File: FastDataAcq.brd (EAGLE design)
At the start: 160 x 100 mm, 225 parts, among them IC1 LT1963AEQ, IC2 FT230XQ, IC3 ADCMP553BRMZ, J1 MICRO-FIT_3.0_2POS_RA_SMD, J2 USB_MICROAB_SMT, X1 87832-14, X2 SMA-142-0701-801/806, X3 SMA-142-0701-801/806, Y1 SI530-500, Y2 100MHz, Y3 DNP

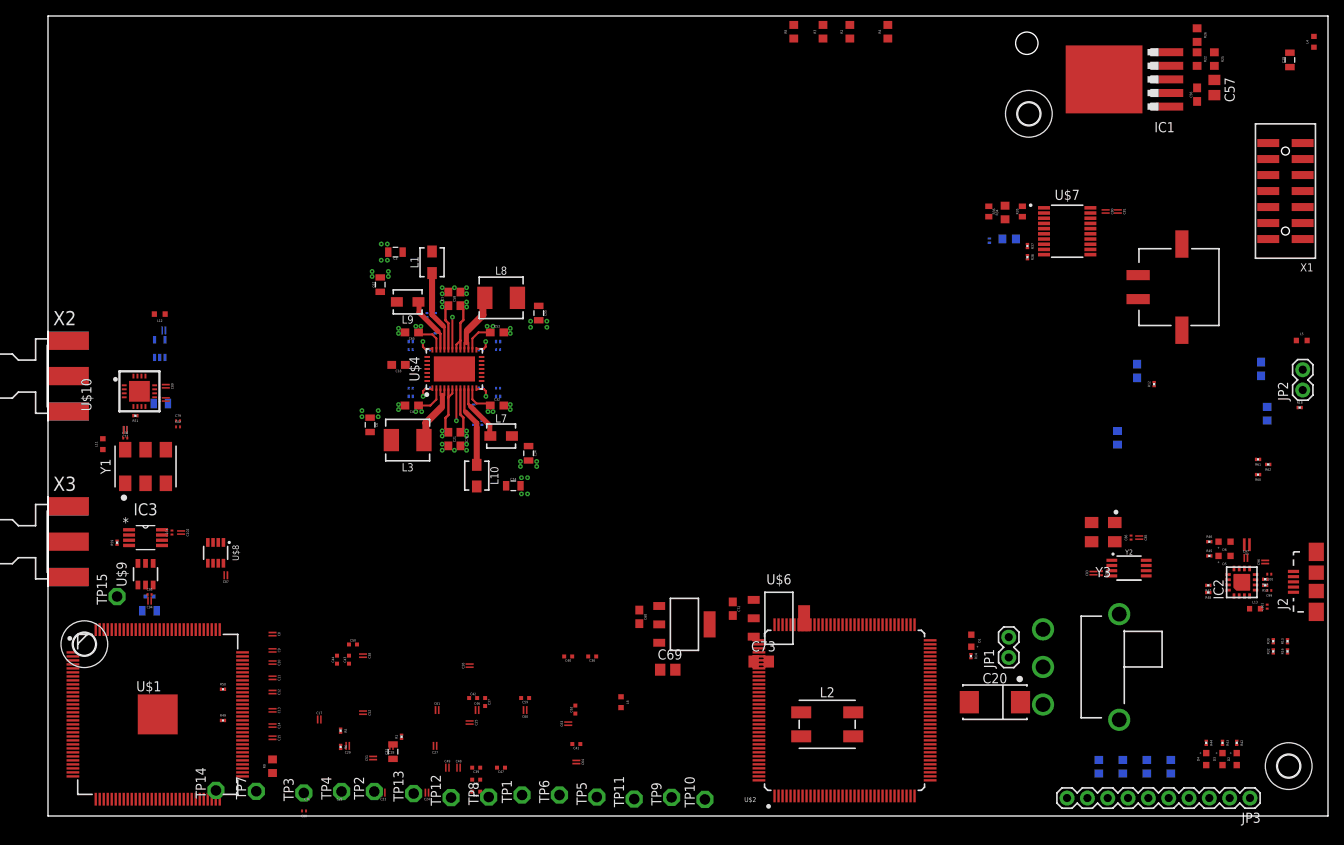
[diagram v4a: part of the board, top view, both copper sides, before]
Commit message: Component placement semi-finalized
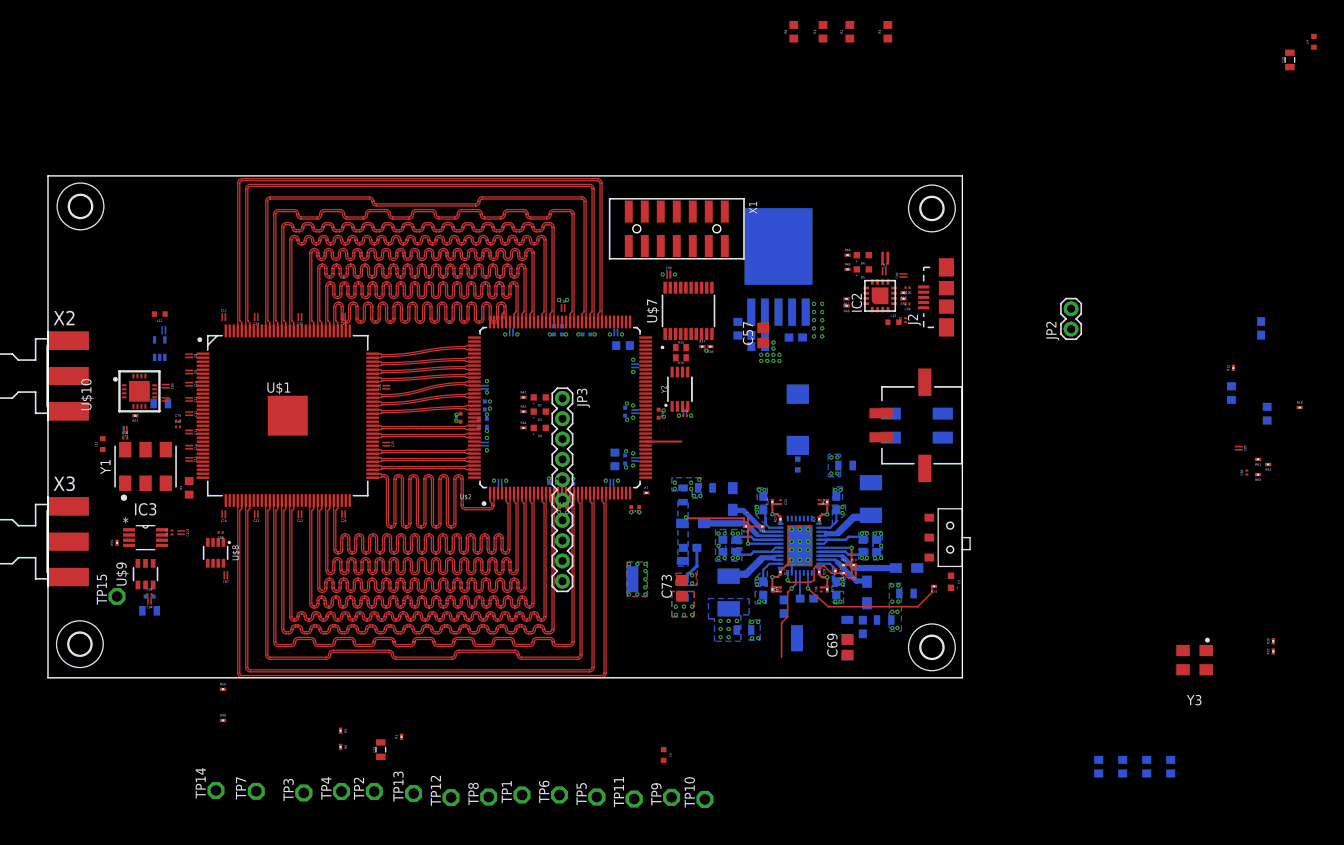
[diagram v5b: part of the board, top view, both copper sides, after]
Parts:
- removed JP1: JUMPER-2PTH, SparkFun-Passives:1X02
- removed U$3: SLIDER_SPDT_1101M2S3AQE2, Schuyler:C_AND_K_1101M2S3AQE2
- added S1: SLIDER_SPDT_AYZ0102AGRLC, Schuyler:AYZ0102AGRLC
- moved H4 166.4 mm to (4.06, 76.2), turned to 0 degrees
- moved H3 135.9 mm to (3.99, 21.5)
- moved H2 119.1 mm to (110.5, 75.9)
- moved JP3 99.4 mm to (64.3, 52.2), turned to 270 degrees
- moved R42 99.1 mm to (59.4, 52.3), turned to 0 degrees
- moved D2 98.2 mm to (61.5, 52.3), turned to 180 degrees
- moved R43 96.7 mm to (59.4, 50.5), turned to 0 degrees
- moved D3 95.8 mm to (61.5, 50.5), turned to 180 degrees
- moved R44 94.0 mm to (59.4, 48.5), turned to 0 degrees
- moved D4 93.0 mm to (61.5, 48.5), turned to 180 degrees
- moved C3 76.8 mm to (107.3, 27.8), flipped to the bottom, turned to 0 degrees
- moved H1 76.4 mm to (110.5, 21.1), flipped to the top
- moved X1 76.2 mm to (78.6, 73.4), turned to 180 degrees
- moved C67 75.7 mm to (104.5, 24.5), flipped to the bottom, turned to 180 degrees
- moved L1 70.6 mm to (107.3, 31.0), flipped to the bottom, turned to 180 degrees
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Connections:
- net N$12 renamed S1EN
- net N$16 renamed S4EN
- removed net N$1: JP1.2, L2.P$4, U$3.P$1
- removed net N$17: C20.P$2, JP1.1, L5.P$1, R14.2, U$3.P$2
- removed net POWER_IN+: J1.P$2, L2.P$1
- removed net POWER_IN-: J1.P$1, L2.P$2
- new net N$24: C20.P$1, L2.P$3, L5.P$1
- new net N$34: J1.P$1, L2.P$1
- new net N$35: J1.P$2, L2.P$2
- new net PWR_ENABLE: R14.2, S1.P$2, U$4.P$13, U$4.P$33
- net GND: now also C20.P$2, L2.P$4, S1.P$1; no longer C20.P$1, L2.P$3
- net VIN: now also S1.P$3; no longer U$4.P$13, U$4.P$33
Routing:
- net DQD0+: track 0.00 -> 90.6 mm
- net DQD0-: track 0.00 -> 90.0 mm
- net DQD1+: track 0.00 -> 86.6 mm
- net DQD1-: track 0.00 -> 86.1 mm
- net DID0+: track 0.00 -> 81.8 mm
- net DID0-: track 0.00 -> 81.3 mm
- net DQD2+: track 0.00 -> 80.9 mm
- net DQD2-: track 0.00 -> 80.4 mm
- net DQ2+: track 0.00 -> 79.7 mm
- net DQD3+: track 0.00 -> 79.6 mm
- net DQ2-: track 0.00 -> 79.4 mm
- net DQD3-: track 0.00 -> 79.1 mm
- net DID1+: track 0.00 -> 78.4 mm
- net DQ1+: track 0.00 -> 78.2 mm
- net DQ0+: track 0.00 -> 78.0 mm
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- added copper zone on layer 16, net 3V3
- added copper zone on layer 1, net 3V3A
- added copper zone on layer 16, net 3V3A
- added copper zone on layer 16, net 3V6_PRE3V3
- added copper zone on layer 1, net GND
- added copper zone on layer 16, net GND
- added copper zone on layer 2, net GND
- added copper zone on layer 16, net VIN
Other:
- board size 160 x 100 mm -> 114.3 x 62.7 mm

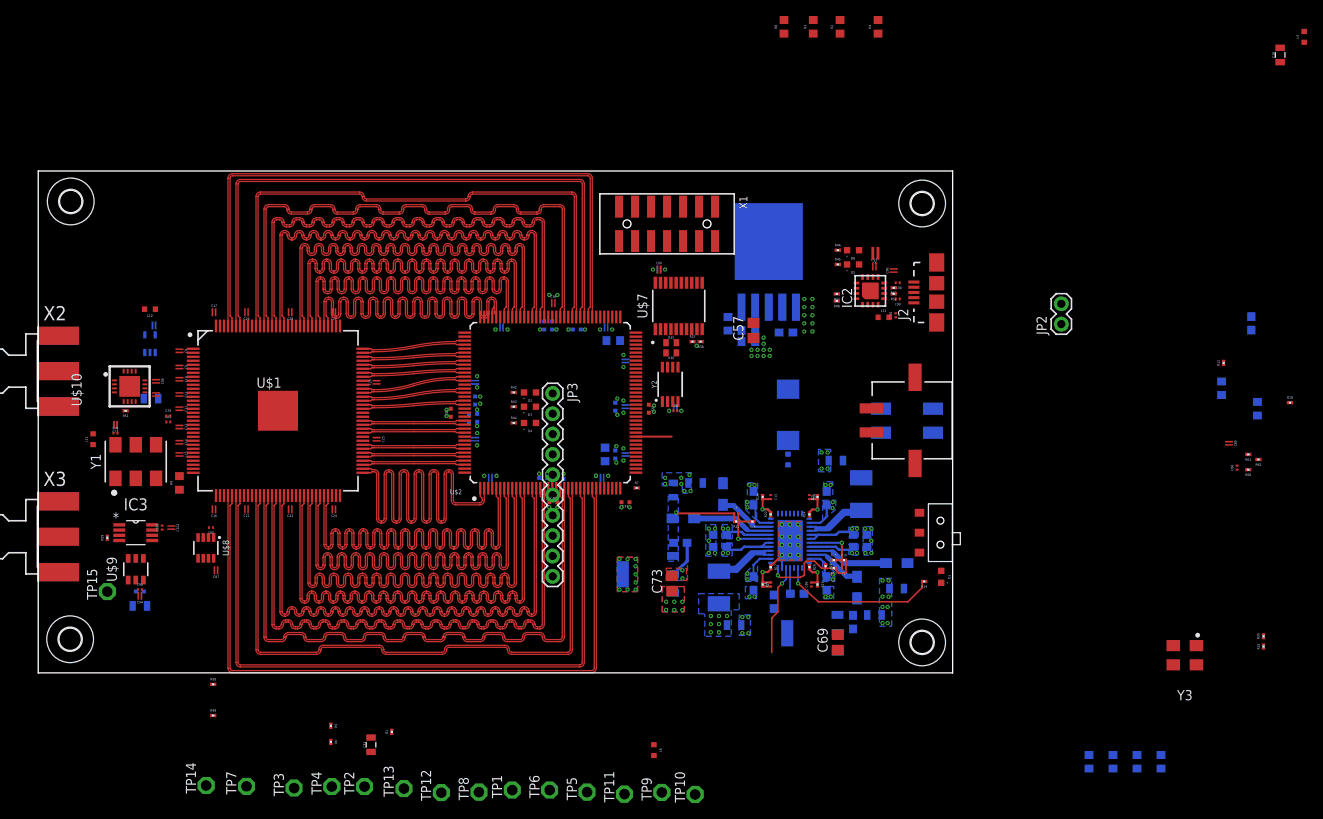
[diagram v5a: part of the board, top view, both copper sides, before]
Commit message: Board layout almost complete.
Power plane almost routes all the power correctly.
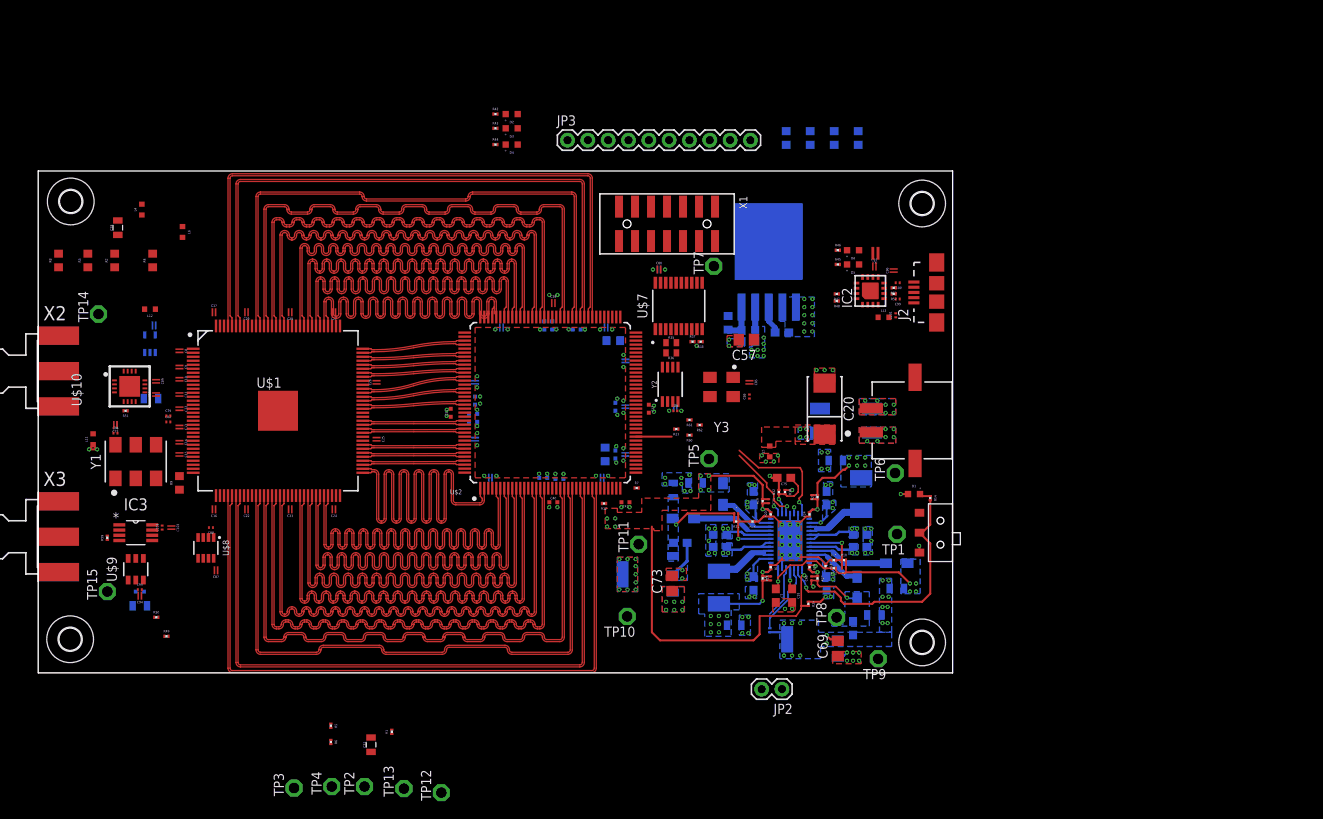
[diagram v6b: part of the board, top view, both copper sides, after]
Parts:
- R23, R28: value NA -> 523K; device rcl:R0603 -> rcl:R0201
- moved C19 146.9 mm to (9.95, 72.9)
- moved L4 146.9 mm to (13.0, 75.2)
- moved R2 95.3 mm to (9.55, 68.8)
- moved R3 95.3 mm to (6.20, 68.8)
- moved R4 95.3 mm to (14.3, 68.8)
- moved R8 95.3 mm to (2.54, 68.8)
- moved L6 87.6 mm to (18.0, 72.4)
- moved TP7 87.4 mm to (84.5, 68.1)
- moved R54 86.7 mm to (99.5, 84.1)
- moved R55 86.7 mm to (96.5, 84.1)
- moved R56 86.7 mm to (93.5, 84.1)
- moved R57 86.7 mm to (102.5, 84.1)
- moved R12 79.4 mm to (70.7, 38.4), turned to 180 degrees
- moved R18 71.0 mm to (91.4, 22.6), flipped to the bottom, turned to 90 degrees
- moved R60 70.0 mm to (81.4, 47.0)
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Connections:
- net N$6 renamed S_MODE
- net S4EN renamed S3EN
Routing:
- net ANALOG_PWR_EN: track 0.00 -> 41.8 mm, vias 0 -> 1
- net GND: track 8.26 -> 37.8 mm, vias 87 -> 106
- net PWR_ENABLE: track 19.8 -> 46.5 mm, vias 1 -> 2
- net 2V8_2V5PRE: track 0.00 -> 22.2 mm, vias 0 -> 3
- net ADC_PWR_EN: track 0.00 -> 14.6 mm, vias 0 -> 1
- net PGOOD: track 0.00 -> 10.3 mm, vias 0 -> 1
- net 1V8: track 0.00 -> 9.75 mm, vias 9 -> 17
- net S_MODE: track 0.00 -> 9.00 mm
- net 1V2: track 3.26 -> 11.8 mm, vias 4 -> 8
- net 3V3: track 1.02 -> 9.18 mm, vias 18 -> 19
- net S3EN: track 0.00 -> 7.44 mm, vias 0 -> 1
- net 2V3_1V9PRE: track 0.00 -> 7.12 mm, vias 10 -> 16
- net S_TEMP: track 11.3 -> 6.59 mm, vias 1 -> 0
- net N$14: track 0.00 -> 4.72 mm
- net 1V9: track 0.00 -> 4.32 mm, vias 0 -> 8
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- added copper zone on layer 1, net 1V2
- added copper zone on layer 16, net 1V2
- added copper zone on layer 3, net 1V2
- added copper zone on layer 1, net 1V8
- added copper zone on layer 16, net 1V8
- added copper zone on layer 3, net 1V8
- added copper zone on layer 16, net 1V9
- added copper zone on layer 3, net 1V9
- added copper zone on layer 3, net 1V9A
- added copper zone on layer 3, net 1V9D
- added copper zone on layer 16, net 2V3_1V9PRE
- added copper zone on layer 3, net 2V3_1V9PRE
- added copper zone on layer 1, net 2V5
- added copper zone on layer 3, net 2V5
- added copper zone on layer 16, net 2V8_2V5PRE
- added copper zone on layer 3, net 3V3
- added copper zone on layer 3, net 3V3A
- added copper zone on layer 1, net N$24
- added copper zone on layer 16, net N$24
- added copper zone on layer 1, net N$34
- added copper zone on layer 16, net N$34
- added copper zone on layer 1, net N$35
- added copper zone on layer 16, net N$35
- added copper zone on layer 1, net VIN
- added copper zone on layer 3, net VIN

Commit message: Continued board layout
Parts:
- removed JP2: JUMPER-2PTH, SparkFun-Passives:1X02
- removed JP3: M10", SparkFun-Connectors:1X10
- added J3: HEADER_0.1"_10P_2R_SMT, Schuyler:HEADER_10P_2R_SMT
- added R40: 0, rcl:R0603
- moved R54 106.8 mm to (14.9, 18.9)
- moved R57 106.7 mm to (17.7, 19.4)
- moved R56 106.2 mm to (9.17, 19.6)
- moved R55 106.0 mm to (12.4, 19.6)
- moved TP13 82.1 mm to (51.3, 84.7)
- moved TP10 72.7 mm to (1.99, 12.1)
- moved TP7 70.7 mm to (15.6, 84.1)
- moved TP4 56.7 mm to (93.2, 8.01)
- moved R42 48.0 mm to (105.2, 86.4)
- moved R43 48.0 mm to (105.2, 84.6)
- moved R44 48.0 mm to (105.2, 82.5)
- moved D2 48.0 mm to (107.2, 86.4)
- moved D3 48.0 mm to (107.2, 84.6)
- moved D4 48.0 mm to (107.2, 82.5)
- moved TP5 40.5 mm to (124.2, 41.5)
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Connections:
- net 3V3: now also J3.P$1; no longer JP3.10
- net FPGA_GPIO1: now also J3.P$9; no longer JP3.2
- net FPGA_GPIO2: now also J3.P$8; no longer JP3.3
- net FPGA_GPIO3: now also J3.P$7; no longer JP3.4
- net FPGA_GPIO4: now also J3.P$6; no longer JP3.5
- net FPGA_GPIO5: now also J3.P$5; no longer JP3.6
- net FPGA_GPIO6: now also J3.P$4; no longer JP3.7
- net FPGA_GPIO7: now also J3.P$3; no longer JP3.8
- net GND: now also J3.P$2; no longer JP3.9
- net S_MODE: now also R40.2; no longer JP2.1
- net VIN: now also R40.1; no longer JP2.2
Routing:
- net ADC_OUTEDGE/DDR/SDATA: track 0.00 -> 56.5 mm, vias 0 -> 1
- net ADC_OUTV/SCLK: track 0.00 -> 54.9 mm, vias 0 -> 1
- net ADC_CALDLY/DES/!SCS: track 0.00 -> 53.4 mm, vias 0 -> 1
- net 2V8_2V5PRE: track 22.2 -> 62.3 mm, vias 3 -> 9
- net 1V8: track 9.75 -> 40.6 mm
- net GND: track 37.8 -> 64.3 mm, vias 106 -> 116
- net FPGA_TDI: track 0.00 -> 22.0 mm, vias 0 -> 1
- net FPGA_TCK: track 0.00 -> 19.2 mm, vias 0 -> 1
- net PWR_ENABLE: track 46.5 -> 59.8 mm
- net FPGA_TMS: track 0.00 -> 13.1 mm, vias 0 -> 1
- net FPGA_TDO: track 0.00 -> 11.8 mm, vias 0 -> 1
- net ADC_PWR_EN: track 14.6 -> 3.28 mm
- net 3V3: track 9.18 -> 19.3 mm, vias 19 -> 21
- net VIN: track 43.0 -> 52.7 mm
- net S_MODE: track 9.00 -> 18.2 mm, vias 0 -> 1
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- removed copper zone on layer 1, net 1V2
